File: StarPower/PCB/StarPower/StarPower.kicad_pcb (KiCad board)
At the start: 2 copper layers, 42 x 14.5 mm, 21 parts, among them SW1 TL3301, U1 ATtiny25-20SSU, U2 SGM809B-SXN3LG, U3 PAM2804AAB010, Y1 32.768 kHz

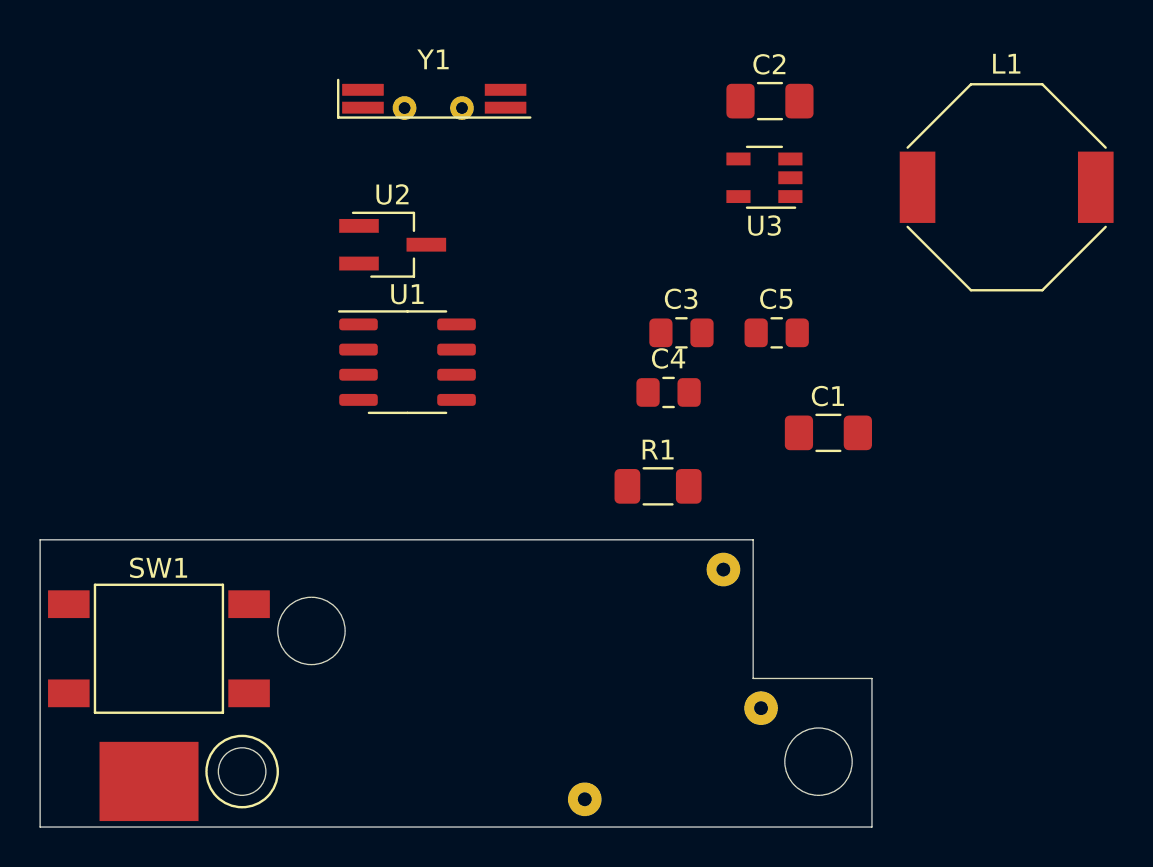
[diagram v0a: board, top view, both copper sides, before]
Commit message: All components are placed, the traces are still missing.
The schematic has some changes:
- Y1 rotated to better fit placement on board
- C5 is now to +BATT instead of +2V8
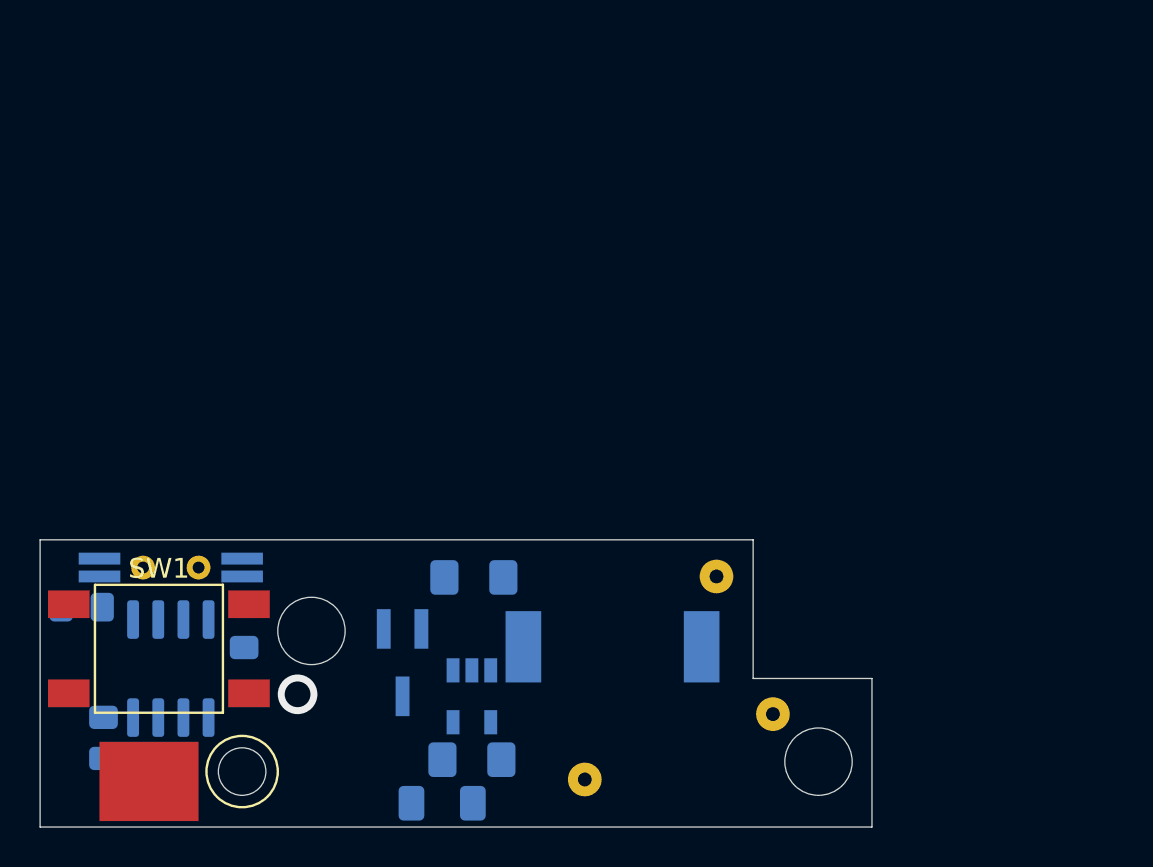
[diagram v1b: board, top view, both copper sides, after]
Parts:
- C1, C2, C3, C4, C5, L1, R1, U1, U2, U3, Y1: moved to B.Cu
- moved C5 39.7 mm to (103.2, 110.0), turned to 270 degrees
- moved C4 31.6 mm to (102.1, 103.4)
- moved L1 30.6 mm to (128.9, 105.4)
- moved U3 30.1 mm to (121.8, 107.9), turned to 270 degrees
- moved C2 28.3 mm to (121.9, 101.9), turned to 180 degrees
- moved Y1 27.2 mm to (106.6, 101.4), turned to 180 degrees
- moved REF** 26.7 mm to (108.0, 101.4), turned to 90 degrees
- moved REF** 26.7 mm to (105.2, 101.4), turned to 90 degrees
- moved C3 26.6 mm to (110.3, 104.4), turned to 90 degrees
- moved C1 24.4 mm to (121.8, 111.1), turned to 180 degrees
- moved U2 21.1 mm to (118.3, 106.2), turned to 270 degrees
- moved U1 19.5 mm to (106.6, 106.5), turned to 270 degrees
- moved R1 19.4 mm to (120.3, 113.3), turned to 180 degrees
- moved REF** 7.72 mm to (137.0, 108.8)
- moved REF** 7.02 mm to (134.2, 101.8)
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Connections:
- C5 pad 1: +2V8 -> +BATT
- Y1 pad 1: /XTAL1 -> /XTAL2
- Y1 pad 2: /XTAL2 -> /XTAL1
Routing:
- net GND: vias 0 -> 1

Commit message: All components are placed.
No, I was not drunk placing microcontroller and its peripherals. :-)
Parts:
- removed the REF** at (108.0, 101.4)
- removed the REF** at (105.2, 101.4)
- added REF**: SolderWire-0.1sqmm_1x01_D0.4mm_OD1mm, Connector_Wire:SolderWire-0.1sqmm_1x01_D0.4mm_OD1mm, F.Cu at (112.0, 109.3)
- added REF**: SolderWire-0.1sqmm_1x01_D0.4mm_OD1mm, Connector_Wire:SolderWire-0.1sqmm_1x01_D0.4mm_OD1mm, F.Cu at (112.9, 108.1)
- Y1: footprint Crystal:Crystal_SMD_SeikoEpson_MC146-4Pin_6.7x1.5mm_HandSoldering -> mibe:Crystal_SMD_Qantek_QTP7-4Pin_6.9x1.4mm_HandSoldering
- moved Y1 9.96 mm to (113.0, 109.0), turned to 325 degrees
- moved C4 8.74 mm to (110.8, 104.2), turned to 270 degrees
- moved C5 8.22 mm to (101.8, 101.9), turned to 235 degrees
- moved C3 5.15 mm to (108.2, 109.1), turned to 55 degrees
- moved U1 2.47 mm to (106.0, 104.1), turned to 145 degrees
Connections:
- net RESET renamed ~RESET
- Y1 pad 1: /XTAL2 -> /XTAL1
- Y1 pad 2: /XTAL1 -> /XTAL2

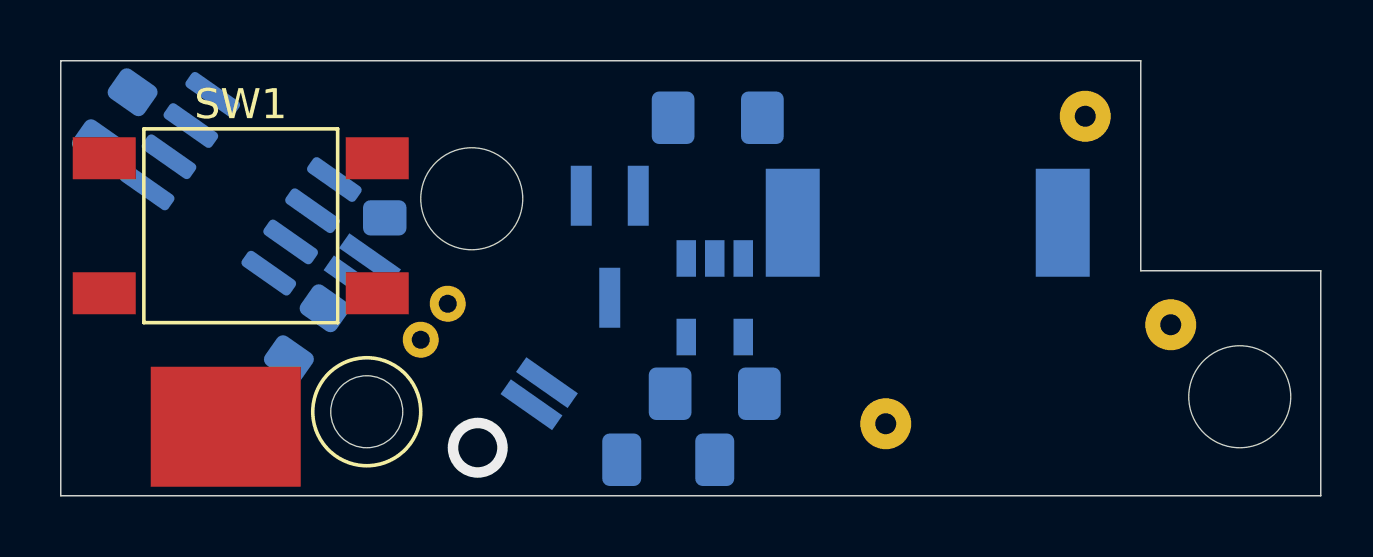
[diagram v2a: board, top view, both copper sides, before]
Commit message: Finish the layout of the first revision.
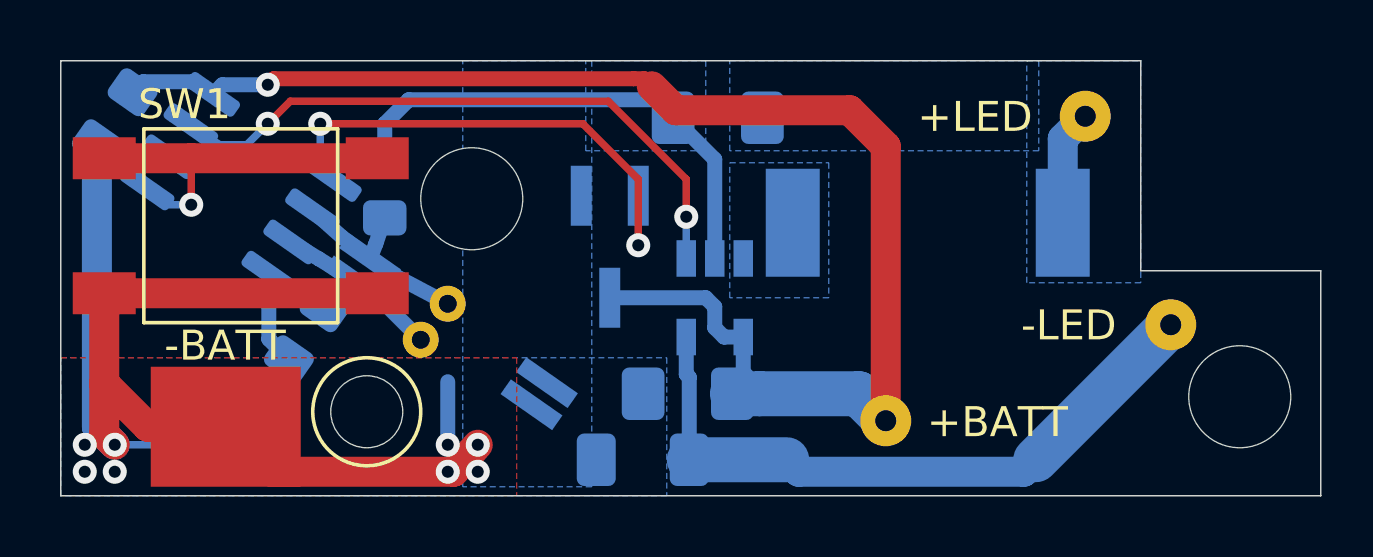
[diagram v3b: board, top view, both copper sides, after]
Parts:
- moved C1 0.90 mm to (120.9, 111.1)
- moved R1 0.85 mm to (119.4, 113.3)
- moved REF** 0.10 mm to (127.5, 112.0)
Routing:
- net GND: track 0.00 -> 67.4 mm, vias 1 -> 8
- net +BATT: track 0.00 -> 48.7 mm, vias 0 -> 1
- net /FB: track 0.00 -> 22.4 mm
- net ENABLE: track 0.00 -> 21.0 mm, vias 0 -> 2
- net ~RESET: track 0.00 -> 17.3 mm, vias 0 -> 2
- net Net-(SW1-Pad1): track 0.00 -> 12.4 mm, vias 0 -> 1
- net /XTAL1: track 0.00 -> 6.95 mm
- net /XTAL2: track 0.00 -> 6.75 mm
- net +2V8: track 0.00 -> 3.93 mm
- added copper zone on B.Cu, net +2V8
- added copper zone on B.Cu, net /SW
- added copper zone on B.Cu, net GND
- added copper zone on F.Cu, net GND
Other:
- board text added: "+BATT"
- board text added: "+LED"
- board text added: "-BATT"
- board text added: "-LED"
- board text added: "Rev. 22/1"
